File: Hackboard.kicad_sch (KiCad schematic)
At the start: 71 parts, among them J1 Conn_01x23_Socket, J2 Micro_SD_Card, J3 Conn_01x31_Socket, J4 Conn_01x08_Socket, J5 Conn_01x02_Pin, J6 USB_C_Receptacle_USB2.0_16P, J7 Barrel_Jack_Switch, Q1 NMOS, Q2 NMOS, Q3 NMOS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

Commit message: Finish tracing all pins, start tracing power
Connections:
- net SD_SCK_24 is gone; now on net SD_SCK_31: J2.5 (CLK), R18.2
- net ANALOG_A6: now also U3.10 (PC2); no longer U3.11 (PC3)
- net ANALOG_A7: now also U3.11 (PC3); no longer U3.10 (PC2)
- net PWM_27: now also R8.1, R9.2
- net PWM_27_O: now also Q1.1 (D)
- net PWM_28: no longer R8.1, R9.2
- net PWM_28_O: no longer Q1.1 (D)
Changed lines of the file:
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@@
 		)
 	)
-	(global_label "SD_SCK_24"
-		(shape bidirectional)
-		(at 149.86 173.99 270)
-		(fields_autoplaced yes)
-		(effects
-			(font
-				(size 1.27 1.27)
-			)
-			(justify right)
-		)
-		(property "Intersheetrefs" "${INTERSHEET_REFS}"
-			(at 149.86 188.6697 90)
-			(effects
-				(font
-					(size 1.27 1.27)
-				)
-				(justify right)
-				(hide yes)
-			)
-		)
-	)
 	(global_label "SD_CS_9_O"
 		(shape bidirectional)
@@
 		)
 	)
-	(global_label "PWM_28_O"
+	(global_label "PWM_27_O"
 		(shape bidirectional)
 		(at 158.75 46.99 270)
@@
 		)
 	)
-	(global_label "ANALOG_A6"
+	(global_label "ANALOG_A7"
 		(shape bidirectional)
 		(at 39.37 80.01 180)
@@
 	(global_label "SD_SCK_31"
 		(shape bidirectional)
+		(at 149.86 173.99 270)
+		(fields_autoplaced yes)
+		(effects
+			(font
+				(size 1.27 1.27)
+			)
+			(justify right)
+		)
+		(property "Intersheetrefs" "${INTERSHEET_REFS}"
+			(at 149.86 188.6697 90)
+			(effects
+				(font
+					(size 1.27 1.27)
+				)
+				(justify right)
+				(hide yes)
+			)
+		)
+	)
+	(global_label "SD_SCK_31"
+		(shape bidirectional)
 		(at 74.93 100.33 0)
 		(fields_autoplaced yes)
@@
 		)
 	)
-	(global_label "ANALOG_A7"
+	(global_label "ANALOG_A6"
 		(shape bidirectional)
 		(at 39.37 77.47 180)
@@
 		)
 	)
-	(global_label "PWM_28"
+	(global_label "PWM_27"
 		(shape bidirectional)
 		(at 152.4 29.21 90)

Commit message: Change connector size, change USB port, add 3d models, add final touches
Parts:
- removed J3: Conn_01x31_Socket, Connector_PinHeader_2.54mm:PinHeader_1x31_P2.54mm_Vertical, symbol Connector:Conn_01x31_Socket
- added J3: Conn_01x32_Socket, symbol Connector:Conn_01x32_Socket
- C1: MPN (none) -> 0603DD106MAT2A
- C10, C13, C17, C18, C3, C6, C8: MPN (none) -> GCM188R71H104KA57D
- C11, C12: MPN (none) -> C1608X5R1A226M080AC
- C14: MPN (none) -> 0603B103K500CT
- C15, C16, C2, C4, C5, C9: MPN (none) -> CC0603KRX7R7BB105
- C7: value 100nF -> 0.1uF; MPN (none) -> GCM188R71H104KA57D
- D1, D3: MPN (none) -> LTST-C190GKT
- D2: MPN (none) -> LTST-C190TBKT
- D4: MPN (none) -> LTST-C191KRKT
- D6: MPN (none) -> VSSAF3L63HM3/H
- F1: MPN (none) -> 0ZCG0050FF2C
- FB1: MPN (none) -> BLM18AG601SN1D
- J1: MPN (none) -> PPTC231LFBN-RC
- J2: MPN (none) -> MSD-1-A
- J6: footprint Connector_USB:USB_C_Receptacle_Molex_216990 -> Connector_USB:USB_C_Receptacle_Amphenol_GSB1C4
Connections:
- net CAN_RX_26_O: now also J3.18 (Pin_18)
- net CAN_TX_25_O: now also J3.19 (Pin_19)
- net GND: now also J3.4 (Pin_4)
- net GPIO_22_O: now also J3.22 (Pin_22)
- net GPIO_23_O: now also J3.21 (Pin_21)
- net GPIO_24_O: now also J3.20 (Pin_20)
- net GPIO_32_O: now also J3.12 (Pin_12)
- net GPIO_33_O: now also J3.11 (Pin_11)
- net GPIO_34_O: now also J3.10 (Pin_10)
- net GPIO_39_O: now also J3.5 (Pin_5)
- net PWM_13_O: now also J3.31 (Pin_31)
- net PWM_14_O: now also J3.30 (Pin_30)
- net PWM_15_O: now also J3.29 (Pin_29)
- net PWM_16_O: now also J3.28 (Pin_28)
- net PWM_19_O: now also J3.25 (Pin_25)
- net PWM_27_O: now also J3.17 (Pin_17)
- net PWM_28_O: now also J3.16 (Pin_16)
- net PWM_29_O: now also J3.15 (Pin_15)
- net PWM_30_O: now also J3.14 (Pin_14)
- net SCL: now also J3.1 (Pin_1)
- net SDA: now also J3.2 (Pin_2)
- net SD_SCK_31_O: now also J3.13 (Pin_13)
- net SPI_CS_PWM_35_O: now also J3.9 (Pin_9)
- net SPI_MISO_36_O: now also J3.8 (Pin_8)
- net SPI_MOSI_37_O: now also J3.7 (Pin_7)
- net SPI_SCK_38_O: now also J3.6 (Pin_6)
- net UART_RX_21_O: now also J3.23 (Pin_23)
- net UART_TX_20_O: now also J3.24 (Pin_24)
- net USB_DM_17_O: now also J3.27 (Pin_27)
- net USB_DP_18_O: now also J3.26 (Pin_26)
- net VDDA: now also J3.3 (Pin_3)
- no-connect marks 5 -> 6

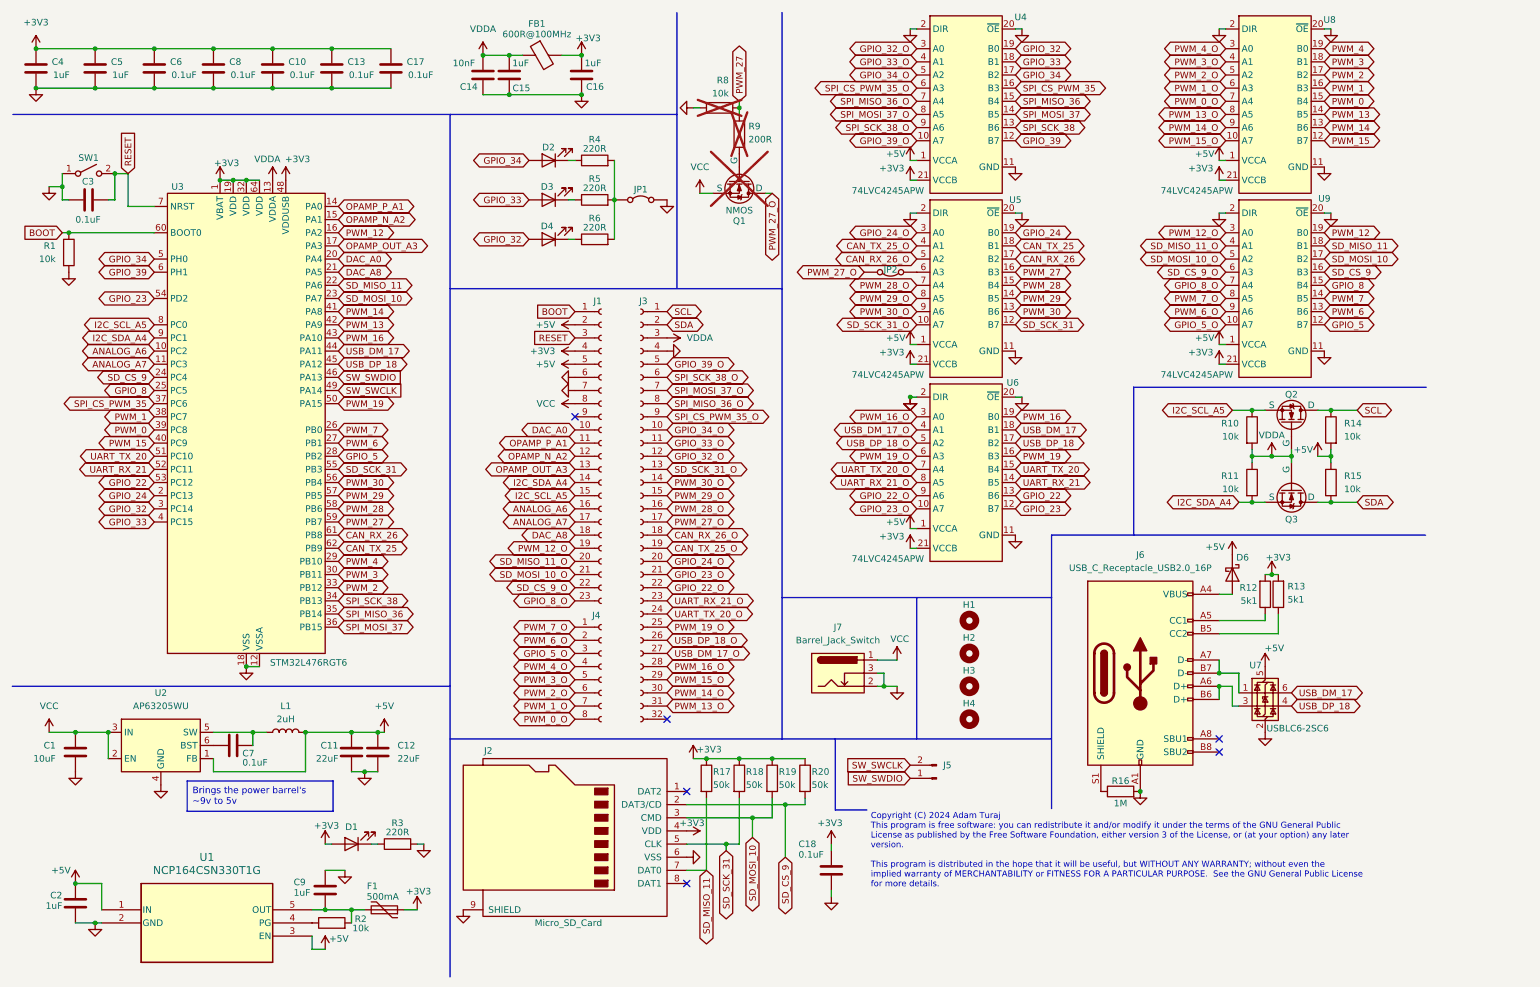
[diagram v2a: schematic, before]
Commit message: Change out LDO, add JLC parts
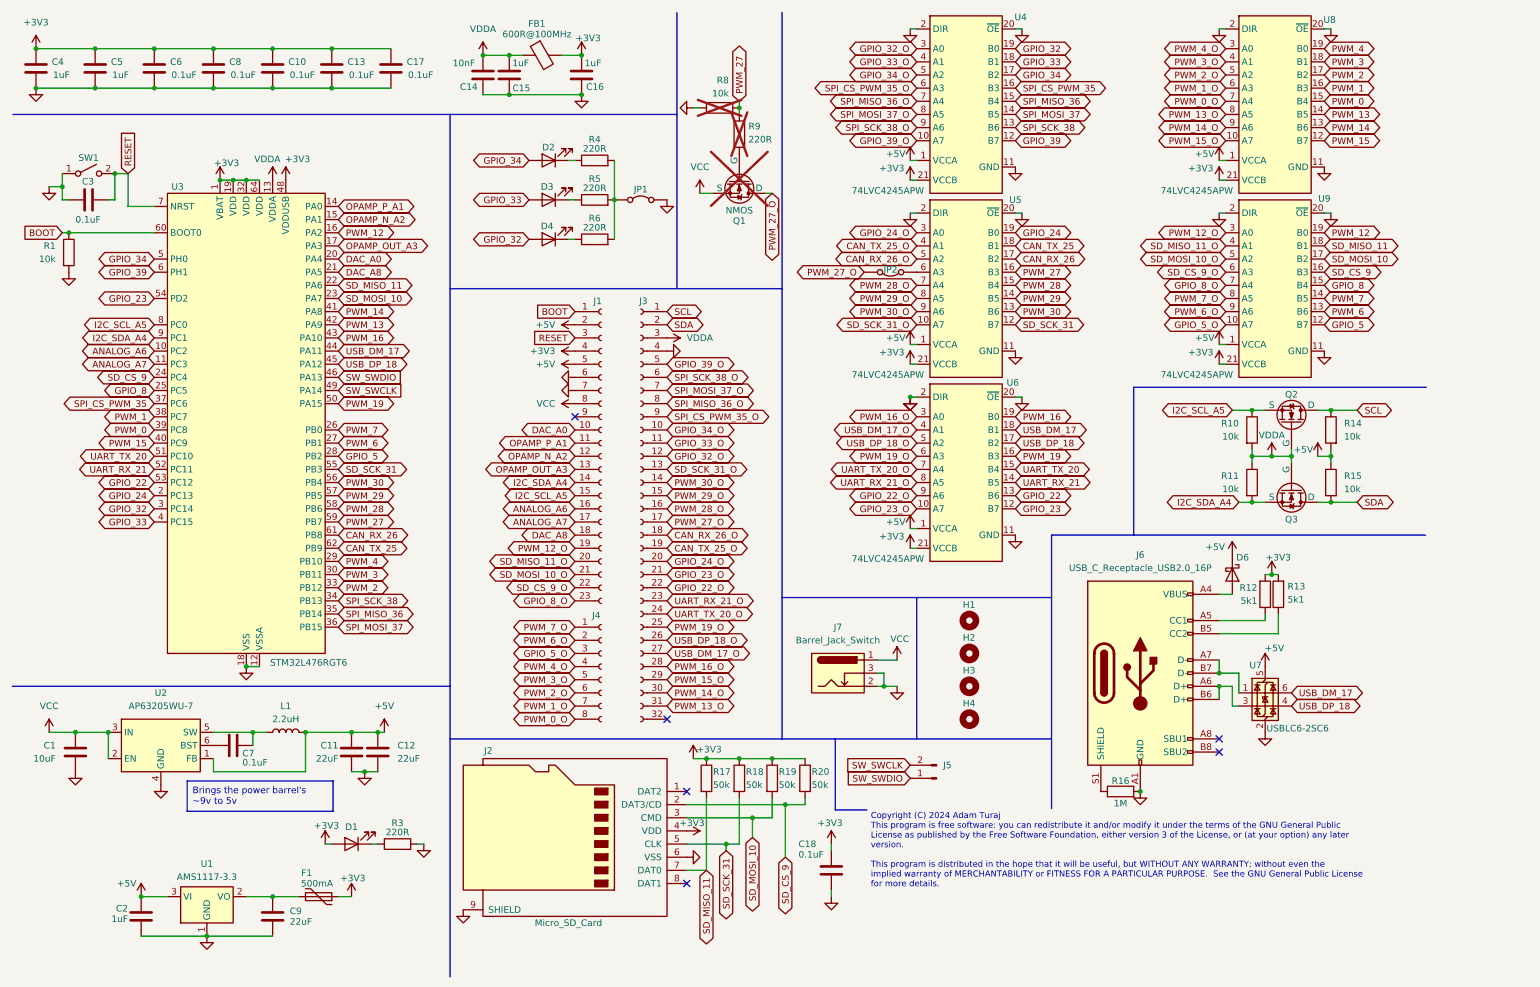
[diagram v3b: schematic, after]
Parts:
- removed R2: 10k, Resistor_SMD:R_0603_1608Metric, symbol Device:R
- removed U1: NCP164CSN330T1G, Package_SO:TSOP-5_1.65x3.05mm_P0.95mm, symbol NCP164CSN:NCP164CSN330T1G
- added U1: AMS1117-3.3, Package_TO_SOT_SMD:SOT-223-3_TabPin2, symbol Regulator_Linear:AMS1117-3.3
- C9: value 1uF -> 22uF
- J3: footprint (none) -> Connector_PinHeader_2.54mm:PinHeader_1x32_P2.54mm_Vertical; MPN (none) -> PPTC231LFBN-RC
- J4: MPN (none) -> PPTC081LFBN-RC
- J5: MPN (none) -> M20-9770246
- J6: MPN (none) -> GSB1C411111DS1HR
- J7: MPN (none) -> PJ-002AH
- L1: value 2uH -> 2.2uH; MPN (none) -> IFSC1515AHER2R2M01
- Q1, Q2, Q3: LCSC (none) -> C15127; MPN (none) -> PMV40UN2R
- R1, R10, R11, R14, R15, R8: MPN (none) -> RMCF0603JT10K0
- R12, R13: MPN (none) -> RC0603FR-075K1L
- R16: MPN (none) -> RMCF0603FT1M00
- R17, R18, R19, R20: MPN (none) -> RT0603BRD0750KL
- R3, R4, R5, R6: MPN (none) -> CRGCQ0603J220R
- R9: value 200R -> 220R; MPN (none) -> CRGCQ0603J220R
- SW1: MPN (none) -> PTS645SK43SMTR92 LFS
- U2: value AP63205WU -> AP63205WU-7; LCSC (none) -> C2071056; MPN (none) -> AP63205WU-7
- U3: LCSC (none) -> C74797; MPN (none) -> STM32L476RGT6
- U4, U5, U6, U8, U9: LCSC (none) -> C7859; MPN (none) -> 74LVC4245APW,118
- U7: LCSC (none) -> C7519; MPN (none) -> USBLC6-2SC6
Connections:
- net +5V: now also U1.3 (VI)
- net GND: now also U1.1 (GND)
- net at C9.2, F1.2: now also U1.2 (VO)
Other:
- moved on the sheet: C2, C9, F1

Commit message: Add some JLC parts
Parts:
- D4: LCSC (none) -> C2286
- D6, FB1: LCSC (none) -> C780074
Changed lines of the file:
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@@
 			)
 		)
-		(property "LCSC" ""
+		(property "LCSC" "C2286"
 			(at 115.57 55.88 0)
 			(effects
@@
 			)
 		)
-		(property "LCSC" ""
+		(property "LCSC" "C780074"
 			(at 114.3 20.32 0)
 			(effects
@@
 			)
 		)
-		(property "LCSC" ""
+		(property "LCSC" "C780074"
 			(at 247.65 120.65 0)
 			(effects
